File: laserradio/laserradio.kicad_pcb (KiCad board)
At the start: 2 copper layers, 84 parts, among them J1 USB4105-GF-A, J2 Conn_01x01_Female, J3 DEBUG, J4 RIGHT, SW1 SW_SPDT, SW2 SW_SPDT, U1 W25Q128JV, U2 RP2040, U3 MCP1702T-3302E_CB, U4 ADA4891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

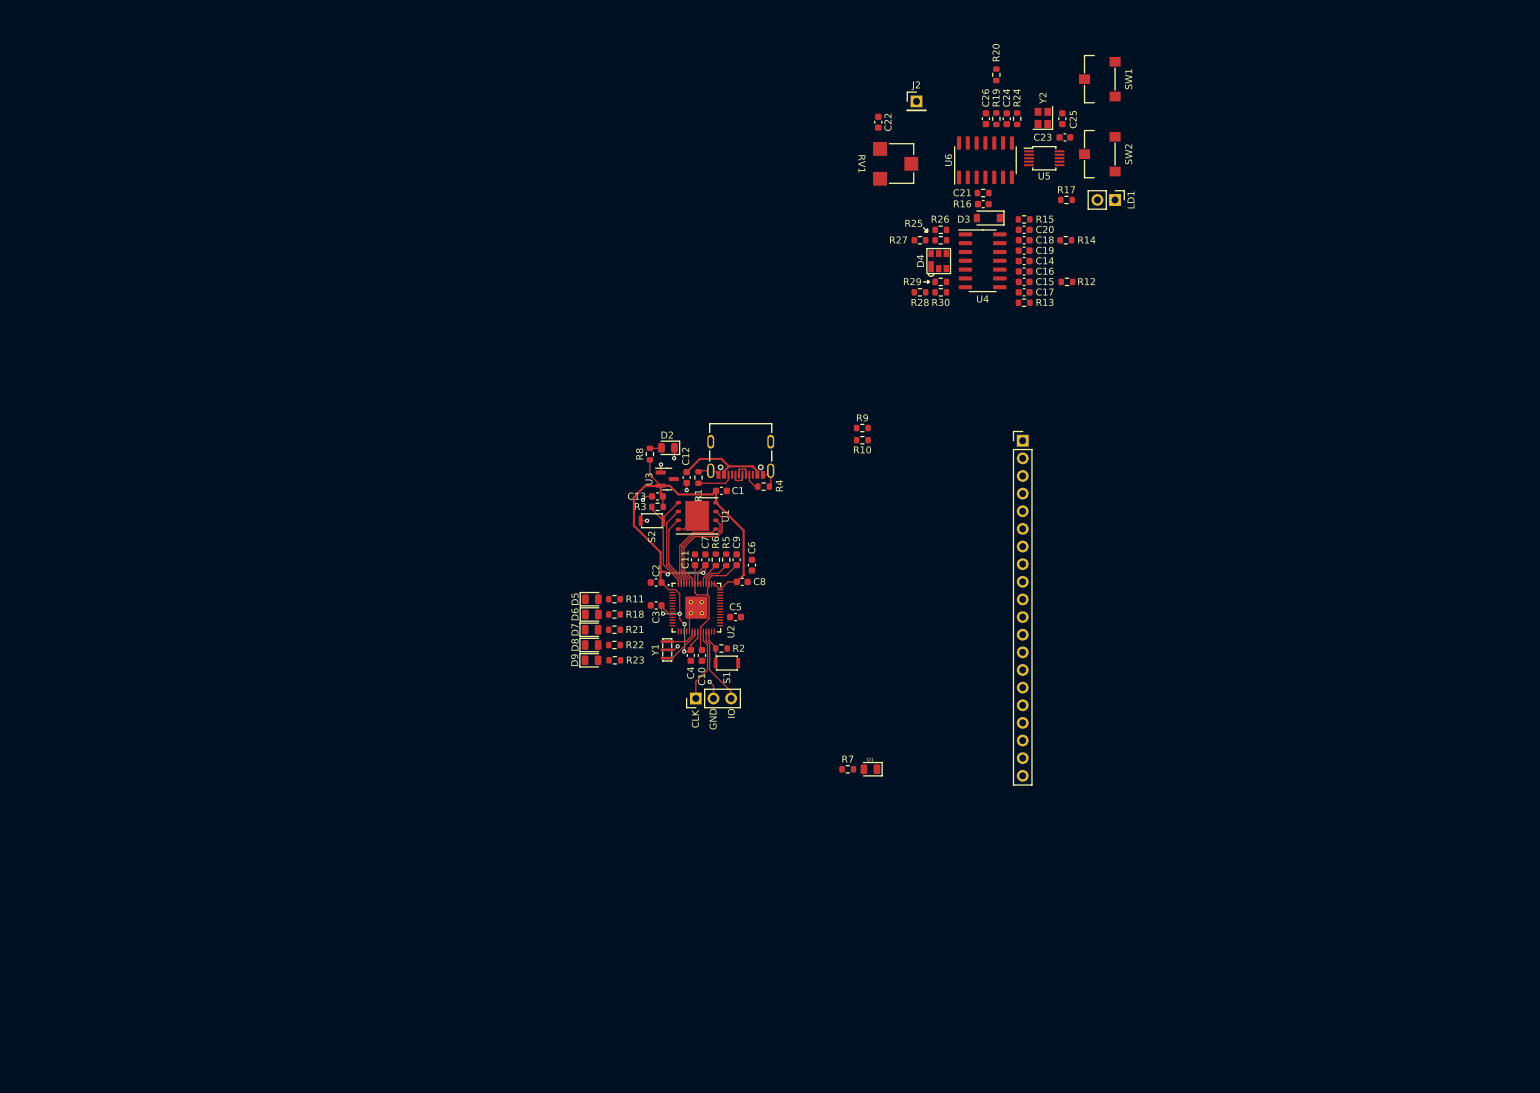
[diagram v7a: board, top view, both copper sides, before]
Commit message: fix voltage divider (adding extra op-amp buffer) on transmit side
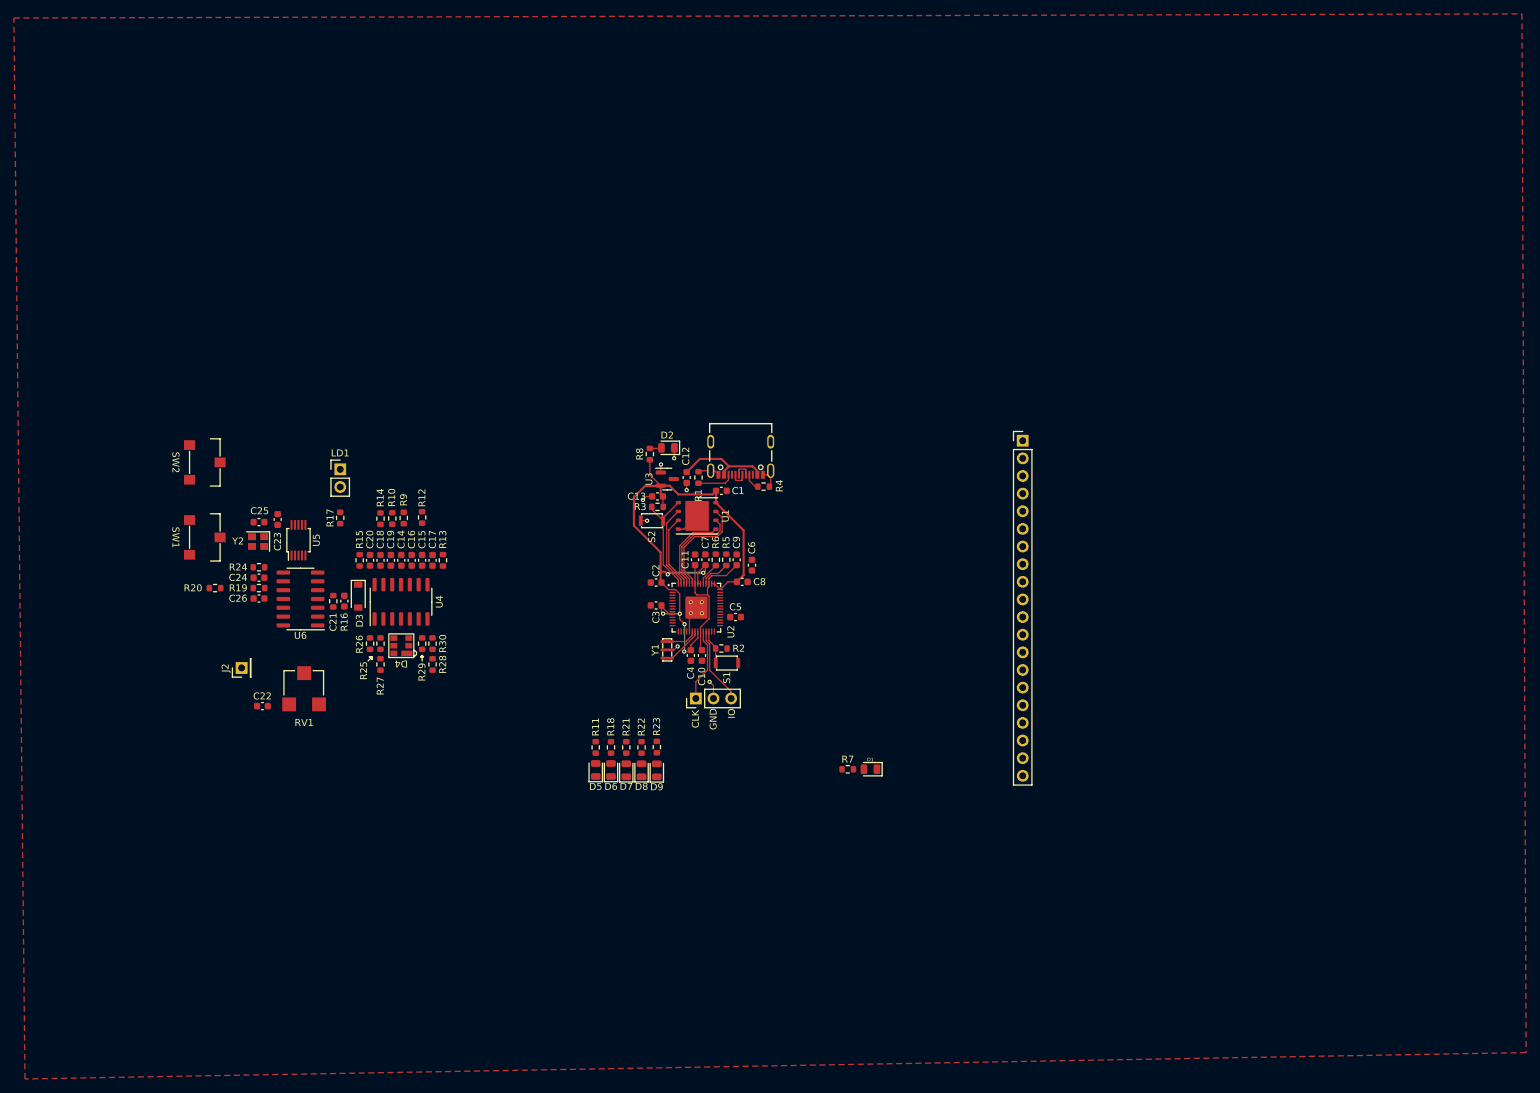
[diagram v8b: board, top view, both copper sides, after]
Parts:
- moved SW1 144.8 mm to (43.5, 89.8), turned to -90 degrees
- moved SW2 136.3 mm to (43.5, 79.0), turned to -90 degrees
- moved R20 134.6 mm to (45.0, 97.1), turned to 180 degrees
- moved C25 129.5 mm to (51.3, 87.6), turned to 180 degrees
- moved Y2 128.4 mm to (51.2, 90.4), turned to 180 degrees
- moved J2 126.9 mm to (48.8, 108.6), turned to 90 degrees
- moved R24 126.9 mm to (51.3, 94.1), turned to 0 degrees
- moved C24 126.4 mm to (51.3, 95.6), turned to 0 degrees
- moved C23 126.0 mm to (54.0, 87.2), turned to 90 degrees
- moved R19 125.9 mm to (51.3, 97.1), turned to 180 degrees
- moved C26 125.4 mm to (51.3, 98.6), turned to 180 degrees
- moved C22 122.2 mm to (51.8, 114.1), turned to 0 degrees
- moved U5 120.7 mm to (57.0, 90.2), turned to 90 degrees
- moved LD1 118.2 mm to (63.0, 80.0), turned to 0 degrees
- moved U6 117.2 mm to (57.3, 98.7), turned to 180 degrees
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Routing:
- added copper zone on F.Cu, net (none)
